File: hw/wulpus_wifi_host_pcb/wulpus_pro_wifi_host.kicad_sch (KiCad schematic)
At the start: 0 parts

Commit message: Linked Footprint and Symbols libraries, added to the KiCAD project
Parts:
- added U1: XIAO-ESP32-C6-SMD, Ultrasound:XIAO-ESP32-C6-SMD, symbol Ultrasound:XIAO-ESP32-C6-SMD
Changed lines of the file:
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@@
 	(generator_version "10.0")
 	(paper "A4")
+	(symbol
+		(lib_id "Ultrasound:XIAO-ESP32-C6-SMD")
+		(at 81.28 77.47 0)
+		(unit 1)
+		(body_style 1)
+		(exclude_from_sim no)
+		(in_bom yes)
+		(on_board yes)
+		(in_pos_files yes)
+		(dnp no)
+		(fields_autoplaced yes)
+		(property "Reference" "U1"
+			(at 92.3133 99.06 0)
+			(show_name no)
+			(do_not_autoplace no)
+			(effects
+				(font
+					(size 1.27 1.27)
+				)
+				(justify left)
+			)
+		)
+		(property "Value" "XIAO-ESP32-C6-SMD"
+			(at 92.3133 101.6 0)
+			(show_name no)
+			(do_not_autoplace no)
+			(effects
+				(font
+					(size 1.27 1.27)
+				)
+				(justify left)
+			)
+		)
+		(property "Footprint" "Ultrasound:XIAO-ESP32-C6-SMD"
+			(at 78.74 72.39 0)
+			(hide yes)
+			(show_name no)
+			(do_not_autoplace no)
+			(effects
+				(font
+					(size 1.27 1.27)
+				)
+			)
+		)
+		(property "Datasheet" ""
+			(at 72.39 72.39 0)
+			(hide yes)
+			(show_name no)
+			(do_not_autoplace no)
+			(effects
+				(font
+					(size 1.27 1.27)
+				)
+			)
+		)
+		(property "Description" ""
+			(at 81.28 77.47 0)
+			(hide yes)
+			(show_name no)
+			(do_not_autoplace no)
+			(effects
+				(font
+					(size 1.27 1.27)
+				)
+			)
+		)
+		(pin "16"
+		)
+		(pin "17"
+		)
+		(pin "5"
+		)
+		(pin "14"
+		)
+		(pin "21"
+		)
+		(pin "6"
+		)
+		(pin "23"
+		)
+		(pin "19"
+		)
+		(pin "22"
+		)
+		(pin "8"
+		)
+		(pin "3"
+		)
+		(pin "7"
+		)
+		(pin "10"
+		)
+		(pin "18"
+		)
+		(pin "11"
+		)
+		(pin "2"
+		)
+		(pin "13"
+		)
+		(pin "1"
+		)
+		(pin "9"
+		)
+		(pin "12"
+		)
+		(pin "15"
+		)
+		(pin "4"
+		)
+		(pin "20"
+		)
+		(pin "24"
+		)
+		(instances
+			(project "wulpus_pro_wifi_host"
+				(path "/939c1465-135d-46db-aee7-7d874dab9895"
+					(reference "U1")
+					(unit 1)
+				)
+			)
+		)
+	)
 	(sheet_instances
 		(path "/"

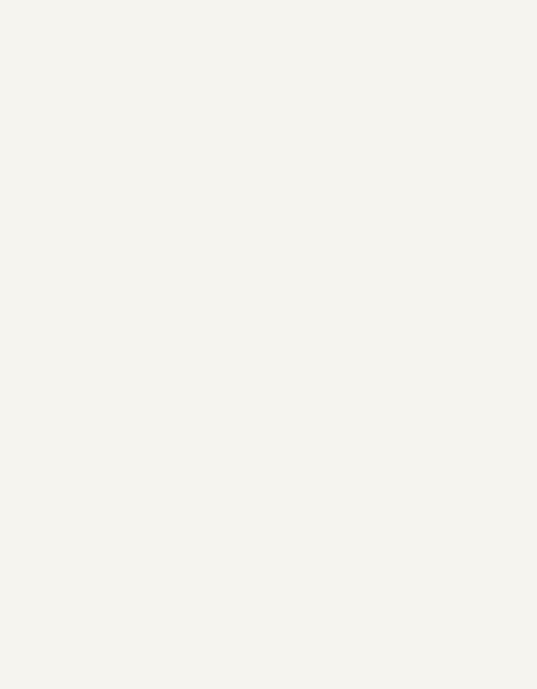
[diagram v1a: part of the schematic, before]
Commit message: Added Hirose host connector, made PCB template
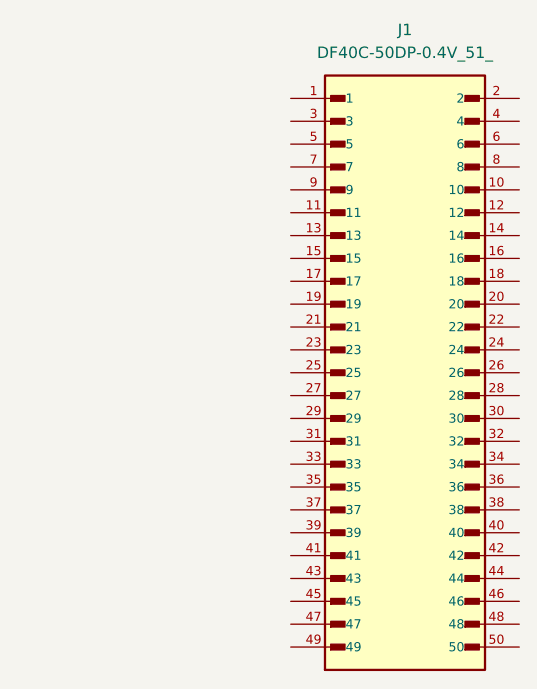
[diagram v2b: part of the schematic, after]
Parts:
- added J1: DF40C-50DP-0.4V_51_, Ultrasound:HIROSE_DF40C-50DP-0.4V_51_, symbol Ultrasound:DF40C-50DP-0.4V_51_

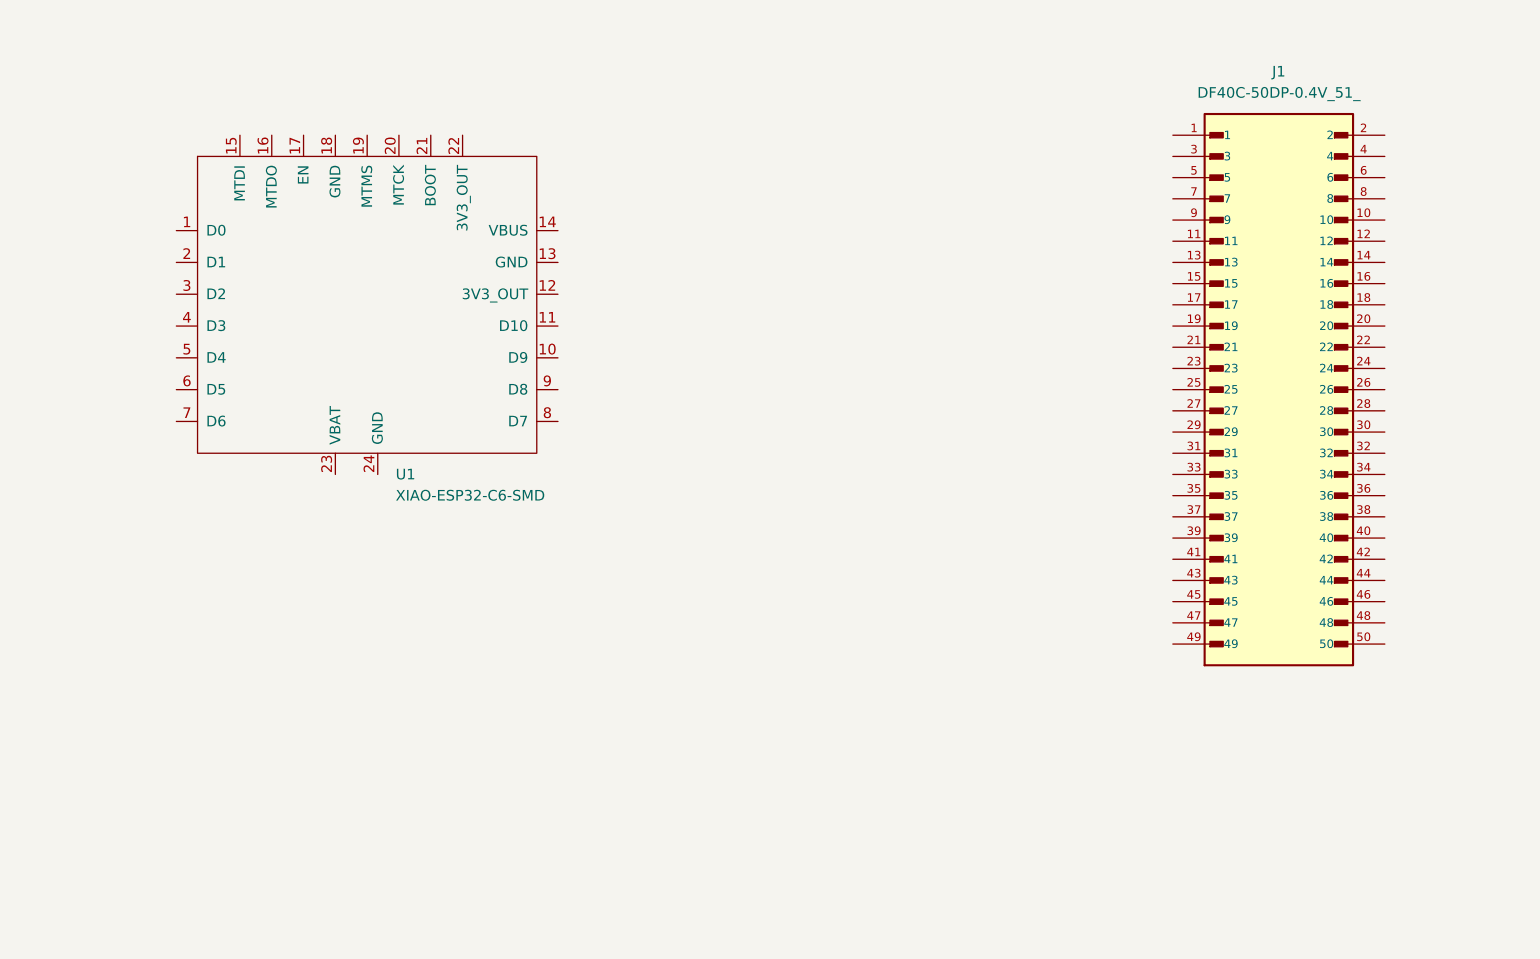
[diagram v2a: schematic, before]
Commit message: Added main ICs to the schematics and layout template
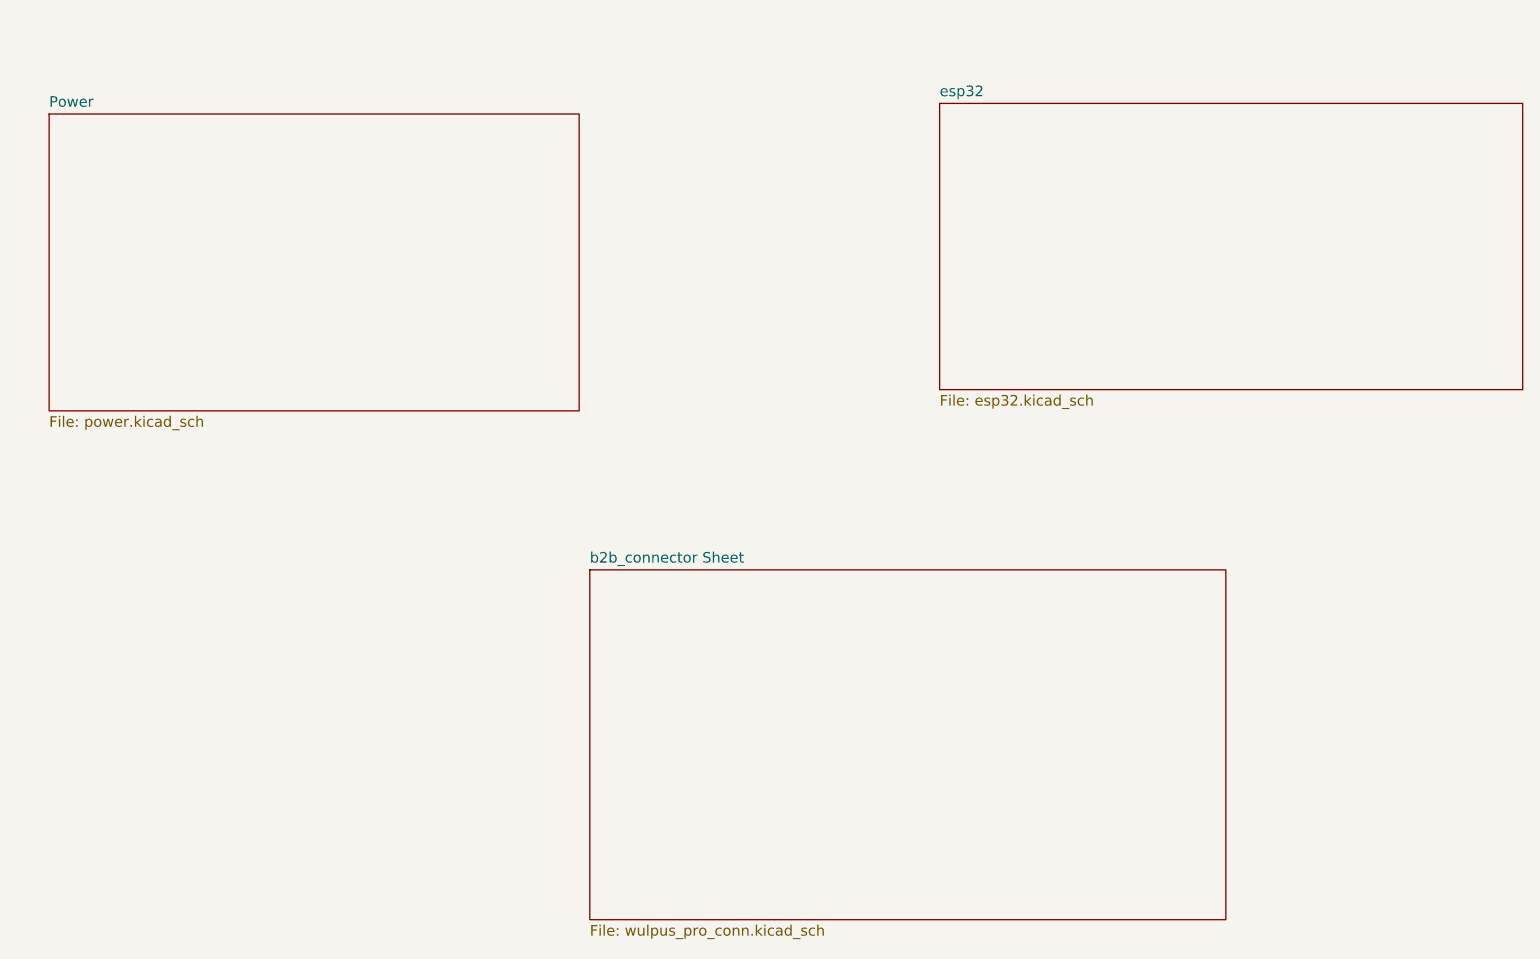
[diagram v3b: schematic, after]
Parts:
- removed J1: DF40C-50DP-0.4V_51_, Ultrasound:HIROSE_DF40C-50DP-0.4V_51_, symbol Ultrasound:DF40C-50DP-0.4V_51_
- removed U1: XIAO-ESP32-C6-SMD, Ultrasound:XIAO-ESP32-C6-SMD, symbol Ultrasound:XIAO-ESP32-C6-SMD
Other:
- added sheet Power (power.kicad_sch)
- added sheet b2b_connector Sheet (wulpus_pro_conn.kicad_sch)
- added sheet esp32 (esp32.kicad_sch)

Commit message: Added hierarchical shets, signals for esp32 and battery protector ref schematic
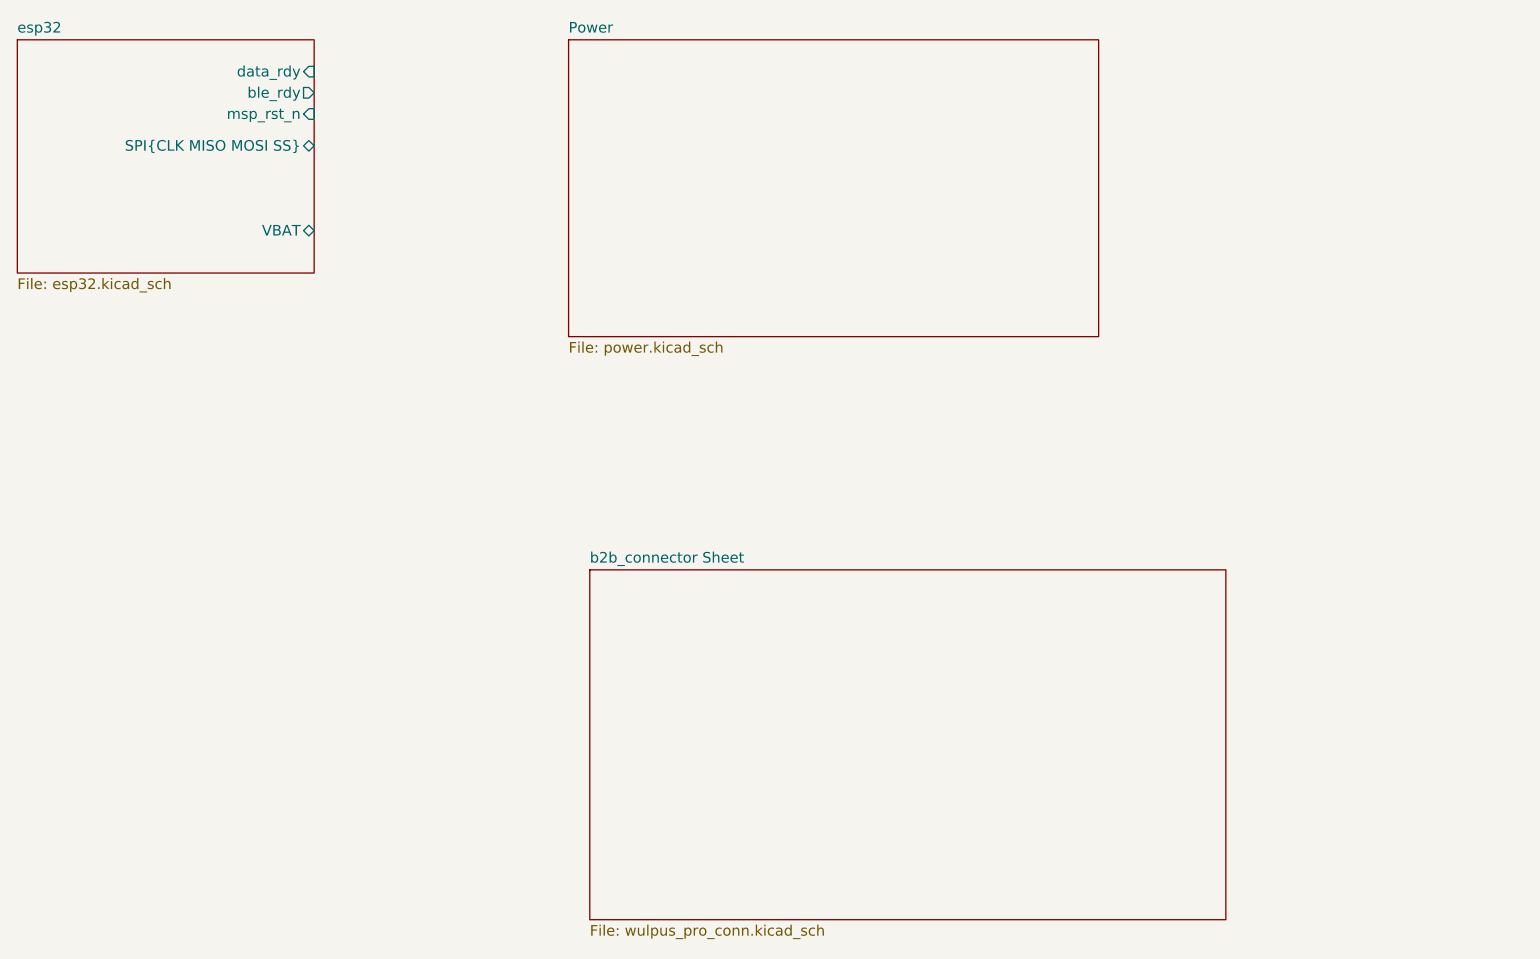
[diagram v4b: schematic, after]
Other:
- sheet esp32 ports: added SPI{CLK MISO MOSI SS}, VBAT, ble_rdy, data_rdy, msp_rst_n; removed none
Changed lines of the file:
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@@
 	(paper "A4")
 	(sheet
-		(at 157.48 54.61)
-		(size 69.85 34.29)
+		(at 46.99 46.99)
+		(size 35.56 27.94)
 		(exclude_from_sim no)
 		(in_bom yes)
@@
 		)
 		(property "Sheetname" "esp32"
-			(at 157.48 53.8984 0)
+			(at 46.99 46.2784 0)
 			(show_name no)
 			(do_not_autoplace no)
@@
 		)
 		(property "Sheetfile" "esp32.kicad_sch"
-			(at 157.48 89.4846 0)
+			(at 46.99 75.5146 0)
 			(show_name no)
 			(do_not_autoplace no)
@@
 				)
 				(justify left top)
+			)
+		)
+		(pin "data_rdy" input
+			(at 82.55 50.8 0)
+			(effects
+				(font
+					(size 1.27 1.27)
+				)
+				(justify right)
+			)
+		)
+		(pin "ble_rdy" output
+			(at 82.55 53.34 0)
+			(effects
+				(font
+					(size 1.27 1.27)
+				)
+				(justify right)
+			)
+		)
+		(pin "msp_rst_n" input
+			(at 82.55 55.88 0)
+			(effects
+				(font
+					(size 1.27 1.27)
+				)
+				(justify right)
+			)
+		)
+		(pin "VBAT" bidirectional
+			(at 82.55 69.85 0)
+			(effects
+				(font
+					(size 1.27 1.27)
+				)
+				(justify right)
+			)
+		)
+		(pin "SPI{CLK MISO MOSI SS}" bidirectional
+			(at 82.55 59.69 0)
+			(effects
+				(font
+					(size 1.27 1.27)
+				)
+				(justify right)
 			)
 		)
@@
 	)
 	(sheet
-		(at 50.8 55.88)
+		(at 113.03 46.99)
 		(size 63.5 35.56)
 		(exclude_from_sim no)
@@
 		)
 		(property "Sheetname" "Power"
-			(at 50.8 55.1684 0)
+			(at 113.03 46.2784 0)
 			(show_name no)
 			(do_not_autoplace no)
@@
 		)
 		(property "Sheetfile" "power.kicad_sch"
-			(at 50.8 92.0246 0)
+			(at 113.03 83.1346 0)
 			(show_name no)
 			(do_not_autoplace no)

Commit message: Updated footprints, mapped 3D models, added layerstack, partial placement and layout
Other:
- sheet Power ports: added VBAT, VBUS; removed none
- sheet b2b_connector Sheet ports: added MSP_JTAG{TEST RST_n TDI TDO TMS TCK}, SPI{CLK MISO MOSI SS}, data_rdy; removed none
- sheet esp32 ports: added MSP_JTAG{TEST RST_n TDI TDO TMS TCK}, VBUS; removed ble_rdy, msp_rst_n
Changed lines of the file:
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@@
 	(generator_version "10.0")
 	(paper "A4")
+	(wire
+		(pts
+			(xy 119.38 111.76) (xy 149.86 111.76)
+		)
+		(stroke
+			(width 0)
+			(type default)
+		)
+	)
+	(wire
+		(pts
+			(xy 119.38 57.15) (xy 149.86 57.15)
+		)
+		(stroke
+			(width 0)
+			(type default)
+		)
+	)
+	(bus
+		(pts
+			(xy 119.38 116.84) (xy 149.86 116.84)
+		)
+		(stroke
+			(width 0)
+			(type default)
+		)
+	)
+	(bus
+		(pts
+			(xy 119.38 121.92) (xy 149.86 121.92)
+		)
+		(stroke
+			(width 0)
+			(type default)
+		)
+	)
+	(wire
+		(pts
+			(xy 119.38 53.34) (xy 149.86 53.34)
+		)
+		(stroke
+			(width 0)
+			(type default)
+		)
+	)
 	(sheet
-		(at 46.99 46.99)
-		(size 35.56 27.94)
+		(at 62.23 48.26)
+		(size 57.15 83.82)
 		(exclude_from_sim no)
 		(in_bom yes)
@@
 		)
 		(property "Sheetname" "esp32"
-			(at 46.99 46.2784 0)
+			(at 62.23 47.5484 0)
 			(show_name no)
 			(do_not_autoplace no)
@@
 		)
 		(property "Sheetfile" "esp32.kicad_sch"
-			(at 46.99 75.5146 0)
+			(at 62.23 132.6646 0)
 			(show_name no)
 			(do_not_autoplace no)
@@
 		)
 		(pin "data_rdy" input
-			(at 82.55 50.8 0)
-			(effects
-				(font
-					(size 1.27 1.27)
-				)
-				(justify right)
-			)
-		)
-		(pin "ble_rdy" output
-			(at 82.55 53.34 0)
-			(effects
-				(font
-					(size 1.27 1.27)
-				)
-				(justify right)
-			)
-		)
-		(pin "msp_rst_n" input
-			(at 82.55 55.88 0)
+			(at 119.38 111.76 0)
 			(effects
 				(font
@@
 		)
 		(pin "VBAT" bidirectional
-			(at 82.55 69.85 0)
+			(at 119.38 57.15 0)
 			(effects
 				(font
@@
 		)
 		(pin "SPI{CLK MISO MOSI SS}" bidirectional
-			(at 82.55 59.69 0)
+			(at 119.38 121.92 0)
+			(effects
+				(font
+					(size 1.27 1.27)
+				)
+				(justify right)
+			)
+		)
+		(pin "MSP_JTAG{TEST RST_n TDI TDO TMS TCK}" bidirectional
+			(at 119.38 116.84 0)
+			(effects
+				(font
+					(size 1.27 1.27)
+				)
+				(justify right)
+			)
+		)
+		(pin "VBUS" output
+			(at 119.38 53.34 0)
 			(effects
 				(font
@@
 			(project "wulpus_pro_wifi_host"
 				(path "/939c1465-135d-46db-aee7-7d874dab9895"
-					(page "3")
+					(page "2")
 				)
 			)
@@
 	)
 	(sheet
-		(at 115.57 110.49)
-		(size 76.2 41.91)
+		(at 149.86 101.6)
+		(size 63.5 30.48)
 		(exclude_from_sim no)
 		(in_bom yes)
@@
 		)
 		(property "Sheetname" "b2b_connector Sheet"
-			(at 115.57 109.7784 0)
+			(at 149.86 100.8884 0)
 			(show_name no)
 			(do_not_autoplace no)
@@
 		)
 		(property "Sheetfile" "wulpus_pro_conn.kicad_sch"
-			(at 115.57 152.9846 0)
+			(at 149.86 132.6646 0)
 			(show_name no)
 			(do_not_autoplace no)
@@
 				)
 				(justify left top)
+			)
+		)
+		(pin "SPI{CLK MISO MOSI SS}" bidirectional
+			(at 149.86 121.92 180)
+			(effects
+				(font
+					(size 1.27 1.27)
+				)
+				(justify left)
+			)
+		)
+		(pin "MSP_JTAG{TEST RST_n TDI TDO TMS TCK}" bidirectional
+			(at 149.86 116.84 180)
+			(effects
+				(font
+					(size 1.27 1.27)
+				)
+				(justify left)
+			)
+		)
+		(pin "data_rdy" output
+			(at 149.86 111.76 180)
+			(effects
+				(font
+					(size 1.27 1.27)
+				)
+				(justify left)
 			)
 		)
@@
 	)
 	(sheet
-		(at 113.03 46.99)
-		(size 63.5 35.56)
+		(at 149.86 48.26)
+		(size 63.5 34.29)
 		(exclude_from_sim no)
 		(in_bom yes)
@@
 		)
 		(property "Sheetname" "Power"
-			(at 113.03 46.2784 0)
+			(at 149.86 47.5484 0)
 			(show_name no)
 			(do_not_autoplace no)
@@
 		)
 		(property "Sheetfile" "power.kicad_sch"
-			(at 113.03 83.1346 0)
+			(at 149.86 83.1346 0)
 			(show_name no)
 			(do_not_autoplace no)
@@
 				)
 				(justify left top)
+			)
+		)
+		(pin "VBAT" bidirectional
+			(at 149.86 57.15 180)
+			(effects
+				(font
+					(size 1.27 1.27)
+				)
+				(justify left)
+			)
+		)
+		(pin "VBUS" input
+			(at 149.86 53.34 180)
+			(effects
+				(font
+					(size 1.27 1.27)
+				)
+				(justify left)
 			)
 		)
@@
 			(project "wulpus_pro_wifi_host"
 				(path "/939c1465-135d-46db-aee7-7d874dab9895"
-					(page "2")
-				)
-			)
+					(page "3")
+				)
+			)

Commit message: Update layer stack, clean up jobset file, PCB and schematics, regenerated outputs
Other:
- title: (none) -> WULPUS PRO WiFi host
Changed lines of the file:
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@@
 	(generator_version "10.0")
 	(paper "A4")
+	(title_block
+		(title "WULPUS PRO WiFi host")
+		(date "2026-08-22")
+		(rev "v1.0.0")
+		(comment 1 "Reviewer: Cedric Hirshi")
+		(comment 2 "Author: Sergei Vostrikov")
+	)
 	(wire
 		(pts

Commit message: Rename project to WULPUS Pro Max
- update user-facing branding across documentation, firmware, and software
- update repository URLs while preserving compatibility identifiers
- release WiFi host PCB v1.0.1 with revised metadata and silkscreen
- regenerate hardware design and fabrication outputs
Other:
- title: WULPUS PRO WiFi host -> WULPUS Pro Max WiFi host
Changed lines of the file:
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@@
 	(paper "A4")
 	(title_block
-		(title "WULPUS PRO WiFi host")
-		(date "2026-08-22")
-		(rev "v1.0.0")
-		(comment 1 "Reviewer: Cedric Hirshi")
+		(title "WULPUS Pro Max WiFi host")
+		(date "2026-09-21")
+		(rev "v1.0.1")
+		(comment 1 "Reviewer: Cedric Hirschi")
 		(comment 2 "Author: Sergei Vostrikov")
 	)
